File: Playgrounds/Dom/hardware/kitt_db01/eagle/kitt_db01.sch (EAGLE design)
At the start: 12 parts, among them Q1 [MMBF170], U1 ADNS-3080, X1 RESON

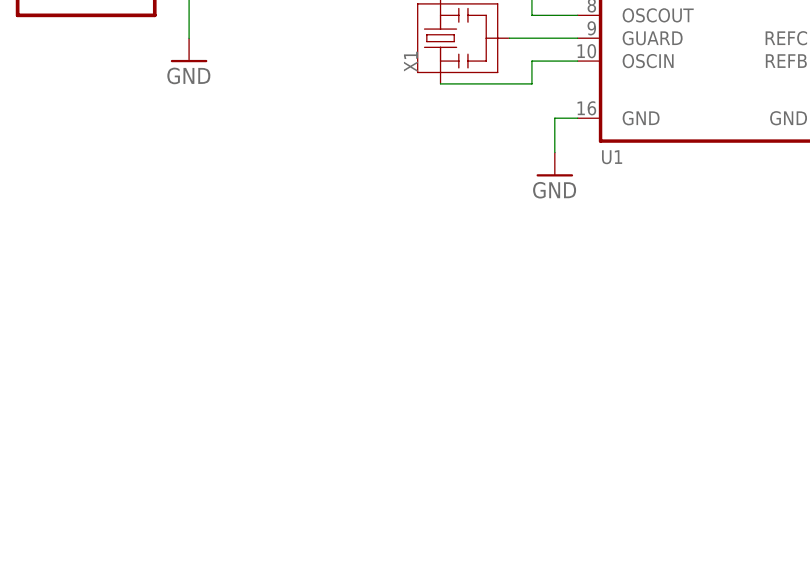
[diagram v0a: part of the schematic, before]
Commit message: rough route and placement completed
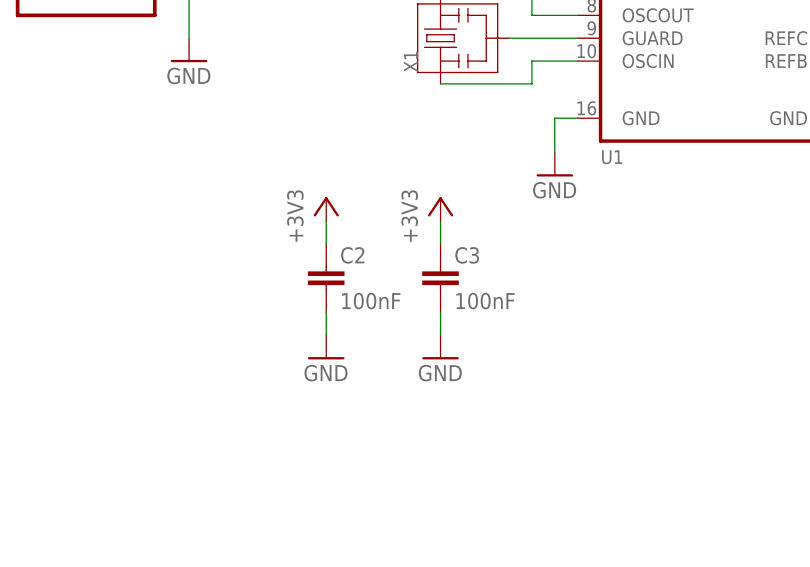
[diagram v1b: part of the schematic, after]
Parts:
- added C2, C3: 100nF, rcl:C-EUC0805K
- R1: device rcl:R-EU_R1206 -> rcl:R-EU_R0805
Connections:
- net +3V3: now also C2.1, C3.1
- net GND: now also C2.2, C3.2
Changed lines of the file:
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@@
 <setting verticaltext="up"/>
 </settings>
-<grid distance="0.05" unitdist="inch" unit="inch" style="lines" multiple="1" display="no" altdistance="0.01" altunitdist="inch" altunit="inch"/>
+<grid distance="0.1" unitdist="inch" unit="inch" style="lines" multiple="1" display="no" altdistance="0.01" altunitdist="inch" altunit="inch"/>
 <layers>
 <layer number="1" name="Top" color="4" fill="1" visible="no" active="no"/>
@@
 <part name="+3V4" library="supply1" deviceset="+3V3" device=""/>
 <part name="R2" library="rcl" deviceset="R-EU_" device="R0805" value="[0R]"/>
-<part name="R1" library="rcl" deviceset="R-EU_" device="R1206" value="180R"/>
+<part name="R1" library="rcl" deviceset="R-EU_" device="R0805" value="180R"/>
 <part name="R3" library="rcl" deviceset="R-EU_" device="R0805" value="[PPR]"/>
 <part name="+3V5" library="supply1" deviceset="+3V3" device=""/>
+<part name="+3V6" library="supply1" deviceset="+3V3" device=""/>
+<part name="GND5" library="supply1" deviceset="GND" device=""/>
+<part name="C2" library="rcl" deviceset="C-EU" device="C0805K" value="100nF"/>
+<part name="+3V7" library="supply1" deviceset="+3V3" device=""/>
+<part name="GND6" library="supply1" deviceset="GND" device=""/>
+<part name="C3" library="rcl" deviceset="C-EU" device="C0805K" value="100nF"/>
 </parts>
 <sheets>
@@
 <instance part="R3" gate="G$1" x="172.72" y="110.49" rot="MR270"/>
 <instance part="+3V5" gate="G$1" x="172.72" y="120.65" rot="MR0"/>
+<instance part="+3V6" gate="G$1" x="101.6" y="63.5"/>
+<instance part="GND5" gate="1" x="101.6" y="45.72"/>
+<instance part="C2" gate="G$1" x="101.6" y="55.88"/>
+<instance part="+3V7" gate="G$1" x="114.3" y="63.5"/>
+<instance part="GND6" gate="1" x="114.3" y="45.72"/>
+<instance part="C3" gate="G$1" x="114.3" y="55.88"/>
 </instances>
 <busses>
@@
 <pinref part="R3" gate="G$1" pin="1"/>
 <wire x1="172.72" y1="118.11" x2="172.72" y2="115.57" width="0.1524" layer="91"/>
+</segment>
+<segment>
+<pinref part="C2" gate="G$1" pin="1"/>
+<pinref part="+3V6" gate="G$1" pin="+3V3"/>
+<wire x1="101.6" y1="60.96" x2="101.6" y2="58.42" width="0.1524" layer="91"/>
+</segment>
+<segment>
+<pinref part="C3" gate="G$1" pin="1"/>
+<pinref part="+3V7" gate="G$1" pin="+3V3"/>
+<wire x1="114.3" y1="60.96" x2="114.3" y2="58.42" width="0.1524" layer="91"/>
 </segment>
 </net>
@@
 <wire x1="194.31" y1="85.09" x2="194.31" y2="68.58" width="0.1524" layer="91"/>
 </segment>
-</net>
+<segment>
+<pinref part="GND5" gate="1" pin="GND"/>
+<pinref part="C2" gate="G$1" pin="2"/>
+<wire x1="101.6" y1="48.26" x2="101.6" y2="50.8" width="0.1524" layer="91"/>
+</segment>
+<segment>
+<pinref part="GND6" gate="1" pin="GND"/>
+<pinref part="C3" gate="G$1" pin="2"/>
+<wire x1="114.3" y1="48.26" x2="114.3" y2="50.8" width="0.1524" layer="91"/>
+</segment>
+</net>

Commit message: Board and Library Updates  - kitt.con.lbr: connectors and connector references    -> DB01 Odometry Board Connector + board outline    -> Arduino Uno shield pins + (pin) overlay for ghostcar  - kitt.ic.lbr: added battery charger component from prev. board
 - mb01.*: motherboard for scaleauto
   -> added board connectors
   -> extended board size and corrected mounting holes
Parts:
- added R4: [PPR], rcl:R-EU_R0805
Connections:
- net !PD: now also R4.1
- net GND: now also R4.2
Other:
- moved on the sheet: C1, LED1, Q1, R1, R2, R3
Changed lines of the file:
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@@
 <setting verticaltext="up"/>
 </settings>
-<grid distance="0.1" unitdist="inch" unit="inch" style="lines" multiple="1" display="no" altdistance="0.01" altunitdist="inch" altunit="inch"/>
+<grid distance="0.05" unitdist="inch" unit="inch" style="lines" multiple="1" display="no" altdistance="0.01" altunitdist="inch" altunit="inch"/>
 <layers>
 <layer number="1" name="Top" color="4" fill="1" visible="no" active="no"/>
@@
 <part name="GND6" library="supply1" deviceset="GND" device=""/>
 <part name="C3" library="rcl" deviceset="C-EU" device="C0805K" value="100nF"/>
+<part name="R4" library="rcl" deviceset="R-EU_" device="R0805" value="[PPR]"/>
+<part name="GND7" library="supply1" deviceset="GND" device=""/>
 </parts>
 <sheets>
@@
 <instance part="+3V3" gate="G$1" x="86.36" y="104.14" rot="MR0"/>
 <instance part="GND3" gate="1" x="86.36" y="78.74"/>
-<instance part="GND4" gate="1" x="194.31" y="66.04"/>
-<instance part="Q1" gate="G$1" x="191.77" y="90.17"/>
-<instance part="LED1" gate="G$1" x="194.31" y="113.03"/>
-<instance part="C1" gate="G$1" x="175.26" y="81.28"/>
-<instance part="+3V4" gate="G$1" x="194.31" y="119.38" rot="MR0"/>
-<instance part="R2" gate="G$1" x="184.15" y="96.52" rot="MR0"/>
-<instance part="R1" gate="G$1" x="194.31" y="102.87" rot="R90"/>
-<instance part="R3" gate="G$1" x="172.72" y="110.49" rot="MR270"/>
-<instance part="+3V5" gate="G$1" x="172.72" y="120.65" rot="MR0"/>
+<instance part="GND4" gate="1" x="215.9" y="66.04"/>
+<instance part="Q1" gate="G$1" x="213.36" y="90.17"/>
+<instance part="LED1" gate="G$1" x="215.9" y="113.03"/>
+<instance part="C1" gate="G$1" x="172.72" y="81.28"/>
+<instance part="+3V4" gate="G$1" x="215.9" y="119.38" rot="MR0"/>
+<instance part="R2" gate="G$1" x="205.74" y="96.52" rot="MR0"/>
+<instance part="R1" gate="G$1" x="215.9" y="102.87" rot="R90"/>
+<instance part="R3" gate="G$1" x="184.15" y="110.49" rot="MR270"/>
+<instance part="+3V5" gate="G$1" x="184.15" y="120.65" rot="MR0"/>
 <instance part="+3V6" gate="G$1" x="101.6" y="63.5"/>
 <instance part="GND5" gate="1" x="101.6" y="45.72"/>
@@
 <instance part="GND6" gate="1" x="114.3" y="45.72"/>
 <instance part="C3" gate="G$1" x="114.3" y="55.88"/>
+<instance part="R4" gate="G$1" x="184.15" y="99.06" rot="MR270"/>
+<instance part="GND7" gate="1" x="184.15" y="66.04"/>
 </instances>
 <busses>
@@
 <pinref part="LED1" gate="G$1" pin="A"/>
 <pinref part="+3V4" gate="G$1" pin="+3V3"/>
-<wire x1="194.31" y1="115.57" x2="194.31" y2="116.84" width="0.1524" layer="91"/>
+<wire x1="215.9" y1="115.57" x2="215.9" y2="116.84" width="0.1524" layer="91"/>
 </segment>
 <segment>
 <pinref part="+3V5" gate="G$1" pin="+3V3"/>
 <pinref part="R3" gate="G$1" pin="1"/>
-<wire x1="172.72" y1="118.11" x2="172.72" y2="115.57" width="0.1524" layer="91"/>
+<wire x1="184.15" y1="118.11" x2="184.15" y2="115.57" width="0.1524" layer="91"/>
 </segment>
 <segment>
@@
 <pinref part="Q1" gate="G$1" pin="S"/>
 <pinref part="GND4" gate="1" pin="GND"/>
-<wire x1="194.31" y1="85.09" x2="194.31" y2="68.58" width="0.1524" layer="91"/>
+<wire x1="215.9" y1="85.09" x2="215.9" y2="68.58" width="0.1524" layer="91"/>
 </segment>
 <segment>
@@
 <wire x1="114.3" y1="48.26" x2="114.3" y2="50.8" width="0.1524" layer="91"/>
 </segment>
+<segment>
+<pinref part="R4" gate="G$1" pin="2"/>
+<pinref part="GND7" gate="1" pin="GND"/>
+<wire x1="184.15" y1="68.58" x2="184.15" y2="93.98" width="0.1524" layer="91"/>
+</segment>
 </net>
 <net name="MOSI" class="0">
@@
 <segment>
 <pinref part="U1" gate="G$1" pin="LEDCTRL"/>
-<wire x1="189.23" y1="87.63" x2="176.53" y2="87.63" width="0.1524" layer="91"/>
+<wire x1="210.82" y1="87.63" x2="198.12" y2="87.63" width="0.1524" layer="91"/>
 <pinref part="Q1" gate="G$1" pin="G"/>
 <pinref part="R2" gate="G$1" pin="2"/>
-<wire x1="176.53" y1="87.63" x2="160.02" y2="87.63" width="0.1524" layer="91"/>
-<wire x1="179.07" y1="96.52" x2="176.53" y2="96.52" width="0.1524" layer="91"/>
-<wire x1="176.53" y1="96.52" x2="176.53" y2="87.63" width="0.1524" layer="91"/>
-<junction x="176.53" y="87.63"/>
+<wire x1="198.12" y1="87.63" x2="160.02" y2="87.63" width="0.1524" layer="91"/>
+<wire x1="200.66" y1="96.52" x2="198.12" y2="96.52" width="0.1524" layer="91"/>
+<wire x1="198.12" y1="96.52" x2="198.12" y2="87.63" width="0.1524" layer="91"/>
+<junction x="198.12" y="87.63"/>
 </segment>
 </net>
@@
 <segment>
 <pinref part="C1" gate="G$1" pin="+"/>
-<wire x1="175.26" y1="83.82" x2="167.64" y2="83.82" width="0.1524" layer="91"/>
+<wire x1="172.72" y1="83.82" x2="167.64" y2="83.82" width="0.1524" layer="91"/>
 <pinref part="U1" gate="G$1" pin="REFC"/>
 <wire x1="167.64" y1="83.82" x2="167.64" y2="81.28" width="0.1524" layer="91"/>
@@
 <segment>
 <pinref part="C1" gate="G$1" pin="-"/>
-<wire x1="175.26" y1="76.2" x2="167.64" y2="76.2" width="0.1524" layer="91"/>
+<wire x1="172.72" y1="76.2" x2="167.64" y2="76.2" width="0.1524" layer="91"/>
 <pinref part="U1" gate="G$1" pin="REFB"/>
 <wire x1="167.64" y1="76.2" x2="167.64" y2="78.74" width="0.1524" layer="91"/>
@@
 <segment>
 <pinref part="Q1" gate="G$1" pin="D"/>
-<wire x1="194.31" y1="97.79" x2="194.31" y2="96.52" width="0.1524" layer="91"/>
+<wire x1="215.9" y1="97.79" x2="215.9" y2="96.52" width="0.1524" layer="91"/>
 <pinref part="R2" gate="G$1" pin="1"/>
-<wire x1="194.31" y1="96.52" x2="194.31" y2="95.25" width="0.1524" layer="91"/>
-<wire x1="189.23" y1="96.52" x2="194.31" y2="96.52" width="0.1524" layer="91"/>
-<junction x="194.31" y="96.52"/>
+<wire x1="215.9" y1="96.52" x2="215.9" y2="95.25" width="0.1524" layer="91"/>
+<wire x1="210.82" y1="96.52" x2="215.9" y2="96.52" width="0.1524" layer="91"/>
+<junction x="215.9" y="96.52"/>
 <pinref part="R1" gate="G$1" pin="1"/>
 </segment>
@@
 </segment>
 <segment>
-<wire x1="160.02" y1="104.14" x2="172.72" y2="104.14" width="0.1524" layer="91"/>
+<wire x1="160.02" y1="104.14" x2="184.15" y2="104.14" width="0.1524" layer="91"/>
 <pinref part="U1" gate="G$1" pin="!PD"/>
-<label x="179.07" y="104.14" size="1.27" layer="95" font="vector" xref="yes"/>
+<label x="200.66" y="104.14" size="1.27" layer="95" font="vector" xref="yes"/>
 <pinref part="R3" gate="G$1" pin="2"/>
-<wire x1="172.72" y1="104.14" x2="179.07" y2="104.14" width="0.1524" layer="91"/>
-<wire x1="172.72" y1="105.41" x2="172.72" y2="104.14" width="0.1524" layer="91"/>
-<junction x="172.72" y="104.14"/>
-</segment>
-</net>
+<wire x1="184.15" y1="104.14" x2="200.66" y2="104.14" width="0.1524" layer="91"/>
+<wire x1="184.15" y1="105.41" x2="184.15" y2="104.14" width="0.1524" layer="91"/>
+<junction x="184.15" y="104.14"/>
+<pinref part="R4" gate="G$1" pin="1"/>
+</segment>
+</net>

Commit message: general improvements for DB01  - optimized the connector layout in regards to the MB01  - as there is more board area, an optional 3V3 LDO was added  - now featuring a power indicator  - added an (optional) input for manual LED control
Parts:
- removed CON1: (no value), pinhead:PINHD-2X5
- added C4, C5: 1uF, rcl:CPOL-EUA/3216-18W
- added D1: MBR0520LT, diode:MBR0520LT
- added LED2: POWER, led:LEDCHIP-LED0805
- added R5, R7: [0R], rcl:R-EU_R0805
- added R6: [PPR], rcl:R-EU_R0805
- added SPI/IO: (no value), con-lstb:MA06-1
- added SUPPLY: (no value), con-lstb:MA04-1
- added U2: MIC5205-3.3YM5TR, kitt.ic:MIC5205-3.3YM5TR
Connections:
- new net !LEDCTRL: R7.2, SPI/IO.6
- new net +5V: D1.A, SUPPLY.3
- new net N$10: R5.2, U2.EN
- new net N$11: LED2.C, R6.1
- new net N$9: C4.+, D1.C, R5.1, U2.IN
- net !CS: now also SPI/IO.1; no longer CON1.3
- net !PD: now also SPI/IO.5; no longer CON1.4
- net +3V3: now also C5.+, LED2.A, SUPPLY.2, U2.OUT; no longer CON1.2
- net GND: now also C4.-, C5.-, R6.2, SUPPLY.4, U2.GND; no longer CON1.10, CON1.6, CON1.8
- net MISO: now also SPI/IO.3; no longer CON1.9
- net MOSI: now also SPI/IO.2; no longer CON1.1
- net N$4: now also R7.1
- net RST: now also SUPPLY.1; no longer CON1.5
- net SCLK: now also SPI/IO.4; no longer CON1.7
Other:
- moved on the sheet: C1, C2, C3, LED1, Q1, R1, R2, R3, R4, U1, X1

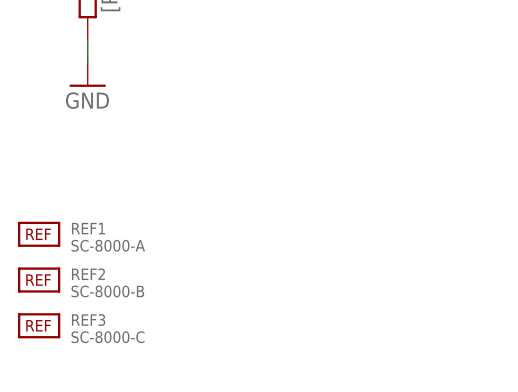
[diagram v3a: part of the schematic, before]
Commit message: updated board dimensions and LED/ADNS3080 placement
still need to figure out the arduino pin situration tough prior to
routing and placement
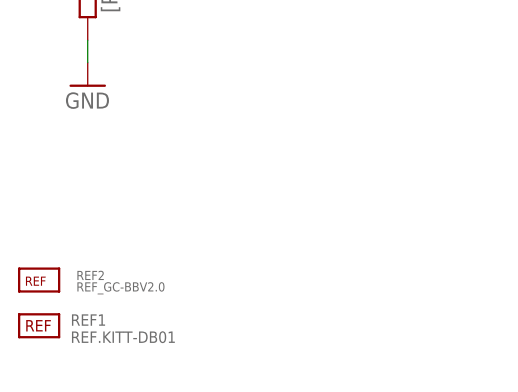
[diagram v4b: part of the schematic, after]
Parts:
- removed REF3: SC-8000-C, scaleauto:SC-8000-C
- LED1: device led:LEDB155 -> led:LED5MM
- REF1: value SC-8000-A -> REF.KITT-DB01; device scaleauto:SC-8000-A -> kitt.refs:REF.KITT-DB01
- REF2: value SC-8000-B -> REF_GC-BBV2.0; device scaleauto:SC-8000-B -> kitt.con:REF_GC-BBV2.0
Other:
- moved on the sheet: REF1
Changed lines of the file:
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@@
 </classes>
 <parts>
-<part name="REF1" library="scaleauto" deviceset="SC-8000-A" device=""/>
-<part name="REF2" library="scaleauto" deviceset="SC-8000-B" device=""/>
-<part name="REF3" library="scaleauto" deviceset="SC-8000-C" device=""/>
 <part name="U1" library="Ai_IC" deviceset="ADNS-3080" device=""/>
 <part name="FRAME1" library="frames" deviceset="A4L-LOC" device=""/>
@@
 <part name="GND4" library="supply1" deviceset="GND" device=""/>
 <part name="Q1" library="transistor-power" deviceset="N-HEXFET-2D_?-*" device="SOT232" value="[MMBF170]"/>
-<part name="LED1" library="led" deviceset="LED" device="B155"/>
+<part name="LED1" library="led" deviceset="LED" device="5MM"/>
 <part name="C1" library="rcl" deviceset="CPOL-EU" device="SMCB"/>
 <part name="+3V4" library="supply1" deviceset="+3V3" device=""/>
@@
 <part name="LED2" library="led" deviceset="LED" device="CHIP-LED0805" value="POWER"/>
 <part name="R7" library="rcl" deviceset="R-EU_" device="R0805" value="[0R]"/>
+<part name="REF1" library="kitt.refs" deviceset="REF.KITT-DB01" device=""/>
+<part name="REF2" library="kitt.con" deviceset="REF_GC-BBV2.0" device=""/>
 </parts>
 <sheets>
@@
 </plain>
 <instances>
-<instance part="REF1" gate="G$1" x="7.62" y="17.78"/>
-<instance part="REF2" gate="G$1" x="7.62" y="12.7"/>
-<instance part="REF3" gate="G$1" x="7.62" y="7.62"/>
 <instance part="U1" gate="G$1" x="160.02" y="106.68"/>
 <instance part="FRAME1" gate="G$1" x="0" y="0"/>
@@
 <instance part="LED2" gate="G$1" x="15.24" y="58.42"/>
 <instance part="R7" gate="G$1" x="220.98" y="96.52" rot="MR180"/>
+<instance part="REF1" gate="G$1" x="7.62" y="7.62"/>
+<instance part="REF2" gate="G$1" x="7.62" y="12.7"/>
 </instances>
 <busses>

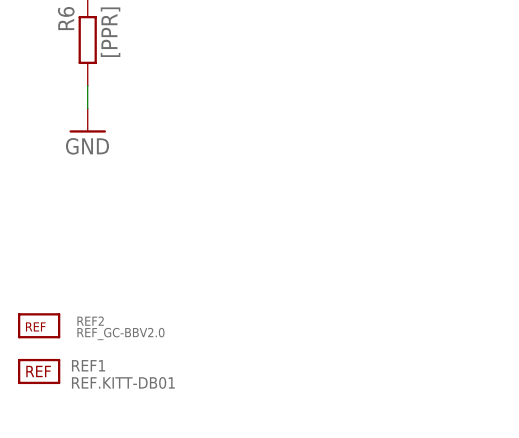
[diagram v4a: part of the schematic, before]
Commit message: updated the placement of the pinheaders and such
beginning now with routing
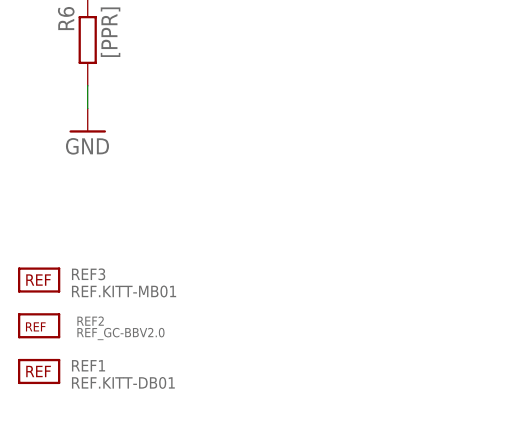
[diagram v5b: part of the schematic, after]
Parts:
- added REF3: REF.KITT-MB01, kitt.refs:REF.KITT-MB01
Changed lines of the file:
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@@
 <part name="REF1" library="kitt.refs" deviceset="REF.KITT-DB01" device=""/>
 <part name="REF2" library="kitt.con" deviceset="REF_GC-BBV2.0" device=""/>
+<part name="REF3" library="kitt.refs" deviceset="REF.KITT-MB01" device=""/>
 </parts>
 <sheets>
@@
 <instance part="REF1" gate="G$1" x="7.62" y="7.62"/>
 <instance part="REF2" gate="G$1" x="7.62" y="12.7"/>
+<instance part="REF3" gate="G$1" x="7.62" y="17.78"/>
 </instances>
 <busses>
